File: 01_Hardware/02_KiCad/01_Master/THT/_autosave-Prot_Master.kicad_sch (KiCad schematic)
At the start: 18 parts, among them J10 Conn_01x22_Female, J20 Conn_01x22_Female, J5 Screw_Terminal_01x04, J6 Screw_Terminal_01x04, U1 LM393P

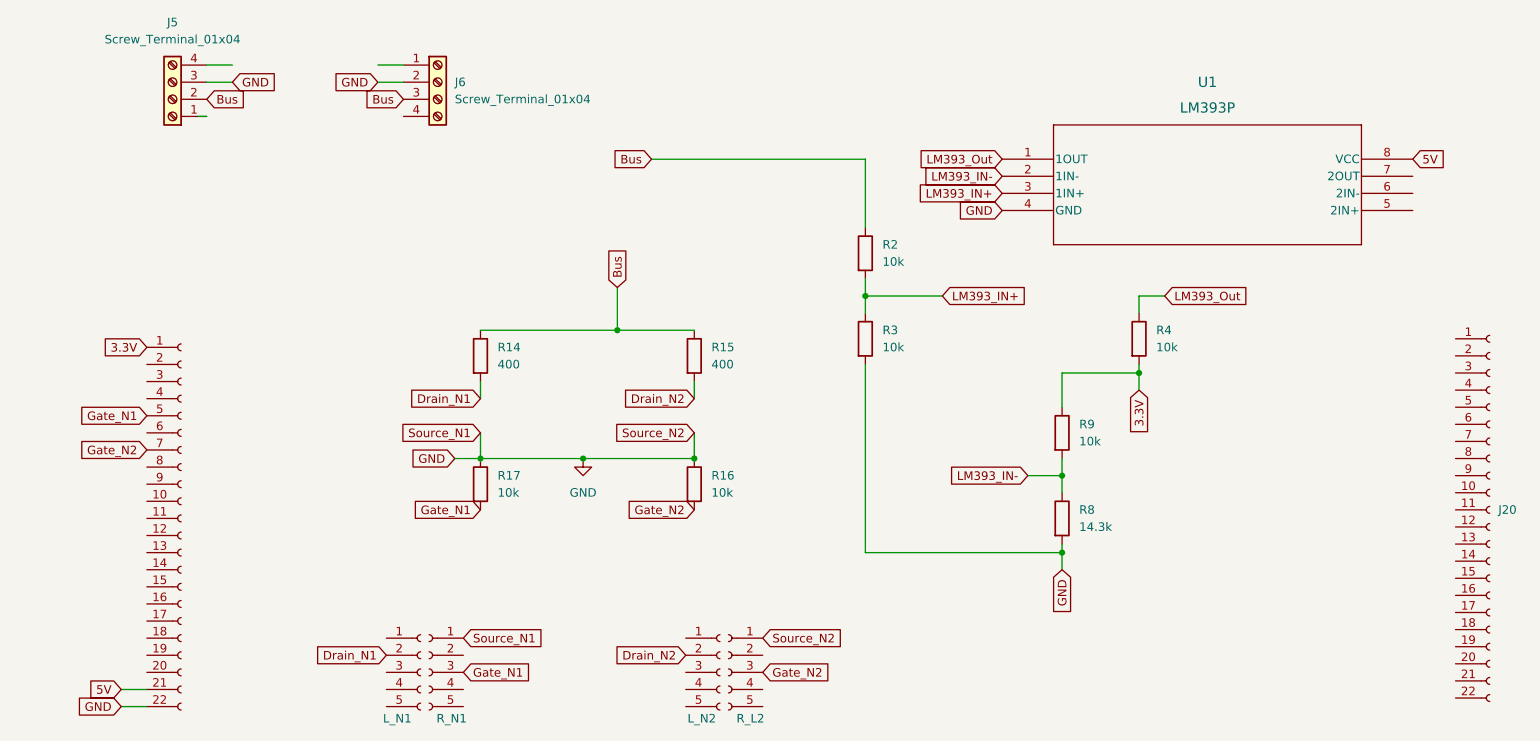
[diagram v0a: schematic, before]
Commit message: Master and Slave Prototyp finsished! JLCPCB ordered
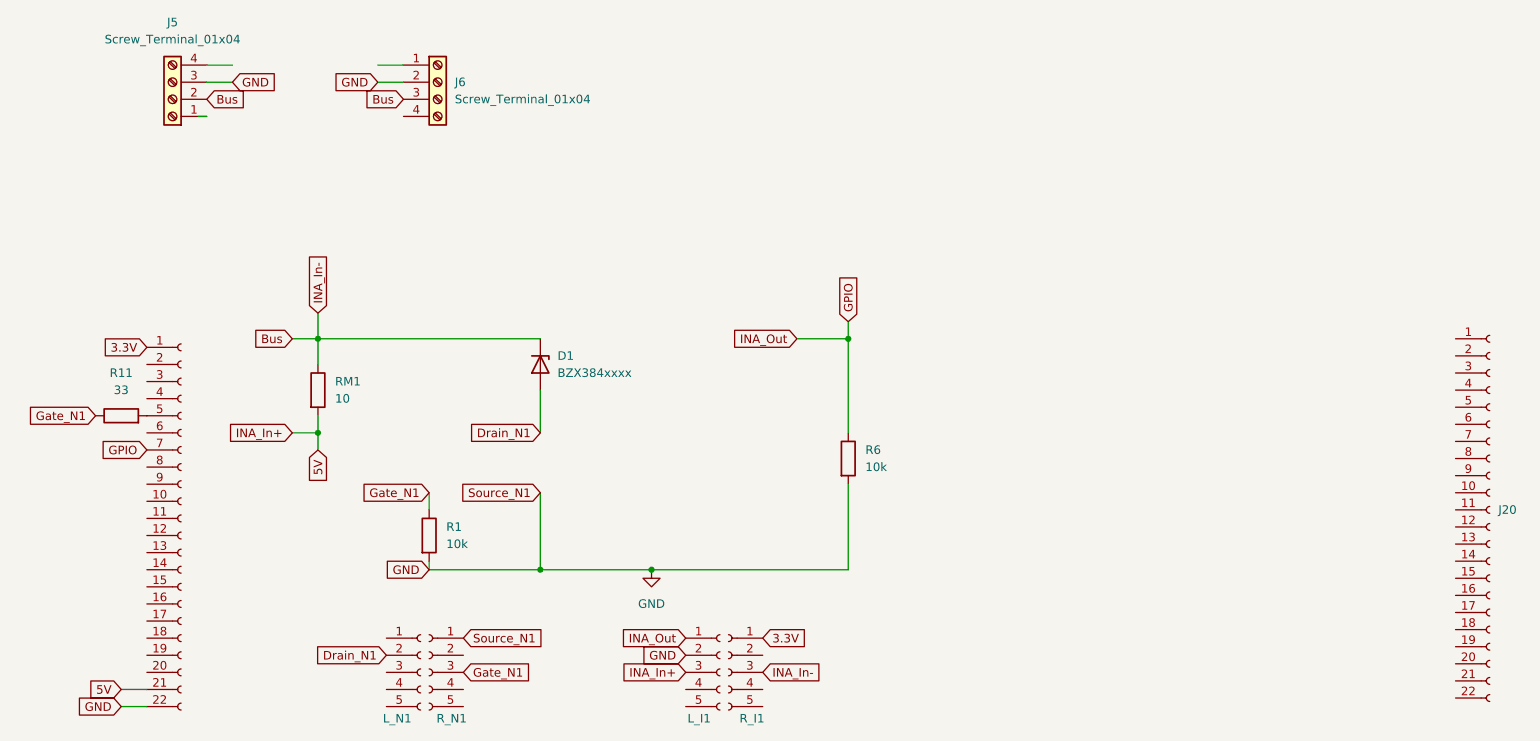
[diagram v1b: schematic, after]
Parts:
- removed R14, R15: 400, Resistor_THT:R_Axial_DIN0204_L3.6mm_D1.6mm_P5.08mm_Horizontal, symbol Device:R
- removed R16, R17, R2, R3, R4, R9: 10k, Resistor_THT:R_Axial_DIN0204_L3.6mm_D1.6mm_P5.08mm_Horizontal, symbol Device:R
- removed R8: 14.3k, Resistor_THT:R_Axial_DIN0204_L3.6mm_D1.6mm_P5.08mm_Horizontal, symbol Device:R
- removed U1: LM393P, LM393:P8, symbol LM393:LM393P
- added D1: BZX384xxxx, Diode_THT:D_A-405_P7.62mm_Horizontal, symbol Diode:BZX384xxxx
- added R1, R6: 10k, Resistor_THT:R_Axial_DIN0204_L3.6mm_D1.6mm_P5.08mm_Horizontal, symbol Device:R
- added R11: 33, Resistor_THT:R_Axial_DIN0204_L3.6mm_D1.6mm_P5.08mm_Horizontal, symbol Device:R
- added RM1: 10, Resistor_THT:R_Axial_DIN0204_L3.6mm_D1.6mm_P5.08mm_Horizontal, symbol Device:R
- renumbered L_N2 to L_I1, R_L2 to R_I1
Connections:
- net Drain_N2 is gone; now on net GND: L_I1.2 (Pin_2)
- net 3.3V: now also R_I1.1 (Pin_1)
- net 5V: now also L_I1.3 (Pin_3), RM1.2
- net Bus: now also R_I1.3 (Pin_3), D1.1 (K), RM1.1
- net Drain_N1: now also D1.2 (A)
- net GND: now also R1.2, R6.2; no longer R_I1.1 (Pin_1)
- net Gate_N1: now also R1.1, R11.1; no longer J10.5 (Pin_5)
- net GPIO: now reaches L_I1.1 (Pin_1)
- net GPIO: now also J10.7 (Pin_7), R6.1
- removed net Gate_N2: J10.7 (Pin_7), R_I1.3 (Pin_3)
- new net: J10.5 (Pin_5), R11.2
